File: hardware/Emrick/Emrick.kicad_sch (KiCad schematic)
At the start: 88 parts, among them J1 LED_STRIP_CONNECTOR, J2 UFL, J3 Conn_02x05_Odd_Even, J4 BATT_CONN, P1 USB_C_Plug_USB2.0, Q1 Q_NMOS_GSD, Q2 Q_NMOS_GSD, Q3 Q_NMOS_GSD, SW1 SW_SPST, SW2 SW_MEC_5E (RESET)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

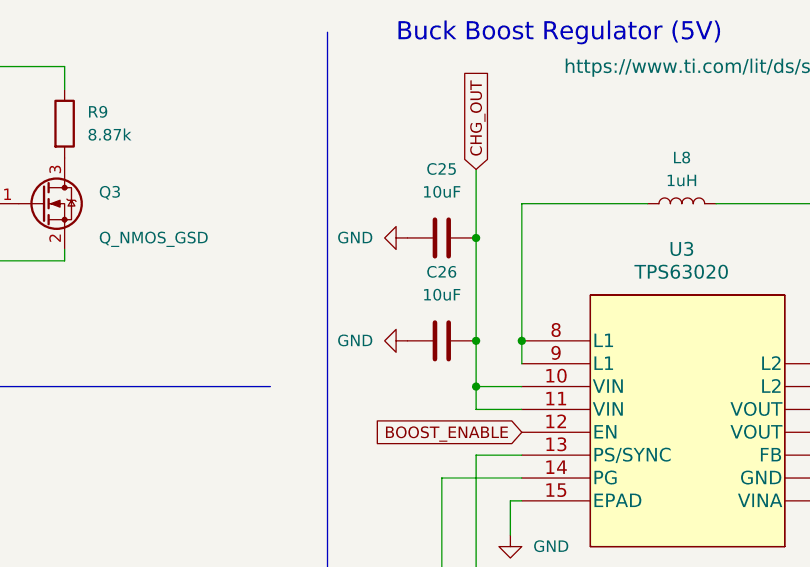
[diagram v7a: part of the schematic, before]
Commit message: update with bigger cap
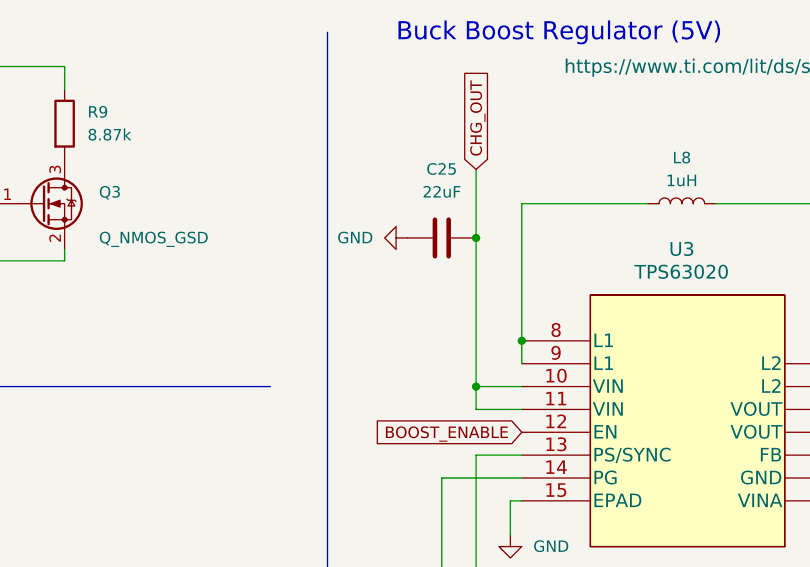
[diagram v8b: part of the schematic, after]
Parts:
- removed C26: 10uF, Capacitor_SMD:C_0402_1005Metric, symbol Device:C
- C25: value 10uF -> 22uF; footprint Capacitor_SMD:C_0402_1005Metric -> Capacitor_SMD:C_0603_1608Metric
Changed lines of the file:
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@@
   (junction (at 387.35 215.9) (diameter 0) (color 0 0 0 0)
   )
-  (junction (at 314.96 205.74) (diameter 0) (color 0 0 0 0)
-  )
   (junction (at 176.53 181.61) (diameter 0) (color 0 0 0 0)
   )
@@
     (stroke (width 0) (type default) (color 0 0 0 0))
   )
-  (wire (pts (xy 314.96 205.74) (xy 314.96 210.82))
+  (wire (pts (xy 314.96 194.31) (xy 314.96 210.82))
     (stroke (width 0) (type default) (color 0 0 0 0))
   )
@@
     (stroke (width 0) (type default) (color 0 0 0 0))
   )
-  (wire (pts (xy 314.96 194.31) (xy 314.96 205.74))
-    (stroke (width 0) (type default) (color 0 0 0 0))
-  )
   (polyline (pts (xy 86.36 43.18) (xy 128.27 43.18))
     (stroke (width 0) (type default) (color 0 0 0 0))
@@
     (in_bom yes) (on_board yes) (fields_autoplaced)
     (property "Reference" "C25" (id 0) (at 311.15 186.69 90))
-    (property "Value" "10uF" (id 1) (at 311.15 189.23 90))
-    (property "Footprint" "Capacitor_SMD:C_0402_1005Metric" (id 2) (at 314.96 193.3448 0)
+    (property "Value" "22uF" (id 1) (at 311.15 189.23 90))
+    (property "Footprint" "Capacitor_SMD:C_0603_1608Metric" (id 2) (at 314.96 193.3448 0)
       (effects (font (size 1.27 1.27)) hide)
     )
@@
     (pin "4")
   )
-  (symbol (lib_id "Device:C") (at 311.15 205.74 90) (unit 1)
-    (in_bom yes) (on_board yes) (fields_autoplaced)
-    (property "Reference" "C26" (id 0) (at 311.15 198.12 90))
-    (property "Value" "10uF" (id 1) (at 311.15 200.66 90))
-    (property "Footprint" "Capacitor_SMD:C_0402_1005Metric" (id 2) (at 314.96 204.7748 0)
-      (effects (font (size 1.27 1.27)) hide)
-    )
-    (property "Datasheet" "~" (id 3) (at 311.15 205.74 0)
-      (effects (font (size 1.27 1.27)) hide)
-    )
-    (pin "1")
-    (pin "2")
-  )
   (symbol (lib_id "Device:R") (at 377.19 220.98 0) (unit 1)
     (in_bom yes) (on_board yes) (fields_autoplaced)
@@
     (pin "2")
   )
-  (symbol (lib_id "power:GND") (at 307.34 205.74 270) (unit 1)
-    (in_bom yes) (on_board yes) (fields_autoplaced)
-    (property "Reference" "#PWR035" (id 0) (at 300.99 205.74 0)
-      (effects (font (size 1.27 1.27)) hide)
-    )
-    (property "Value" "GND" (id 1) (at 303.53 205.7399 90)
-      (effects (font (size 1.27 1.27)) (justify right))
-    )
-    (property "Footprint" "" (id 2) (at 307.34 205.74 0)
-      (effects (font (size 1.27 1.27)) hide)
-    )
-    (property "Datasheet" "" (id 3) (at 307.34 205.74 0)
-      (effects (font (size 1.27 1.27)) hide)
-    )
-    (pin "1")
-  )
   (symbol (lib_id "Device:C") (at 246.38 121.92 90) (unit 1)
     (in_bom yes) (on_board yes)
@@
       (reference "#PWR034") (unit 1) (value "GND") (footprint "")
     )
-    (path "/bdccf2dc-37f0-43eb-a4ca-d61df2cbc91a"
-      (reference "#PWR035") (unit 1) (value "GND") (footprint "")
-    )
     (path "/b05b3162-095d-40cc-95c4-b3c0e80bd3af"
       (reference "#PWR036") (unit 1) (value "GND") (footprint "")
@@
     )
     (path "/4bc490c1-7683-452a-b6a5-9c11f3d97e0a"
-      (reference "C25") (unit 1) (value "10uF") (footprint "Capacitor_SMD:C_0402_1005Metric")
-    )
-    (path "/6e8ab1e4-b3f0-4721-8f2c-85e8d9f16d4e"
-      (reference "C26") (unit 1) (value "10uF") (footprint "Capacitor_SMD:C_0402_1005Metric")
+      (reference "C25") (unit 1) (value "22uF") (footprint "Capacitor_SMD:C_0603_1608Metric")
     )
     (path "/bb636c28-c1cb-492a-b114-66c3929cc704"
